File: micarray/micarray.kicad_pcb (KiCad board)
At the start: 4 copper layers, 75 x 75 mm, 36 parts, among them IC1 74LCX125MTCX, J1 Previous, J2 Next, J3 MCHStreamer J3

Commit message: mounting hole
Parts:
- added C11: 20p, Capacitor_SMD:C_0603_1608Metric_Pad1.08x0.95mm_HandSolder, F.Cu at (90.7, 61.6)
- J3: footprint Connector_PinHeader_2.54mm:PinHeader_2x06_P2.54mm_Horizontal -> Connector_PinHeader_2.54mm:PinHeader_2x06_P2.54mm_Vertical
- moved C6 11.0 mm to (120.9, 42.6), turned to -90 degrees
- moved C5 10.6 mm to (119.4, 42.6), turned to -90 degrees
- moved L3 10.5 mm to (117.9, 42.6), turned to 90 degrees
- moved R5 0.83 mm to (117.8, 46.2)
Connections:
- C1 pad 2: Net-(MK1-SELECT) -> Net-(MK1-VDD)
- C2 pad 2: Net-(MK1-SELECT) -> Net-(MK1-VDD)
- C3 pad 2: Net-(MK2-VDD) -> Net-(MK2-SELECT)
- C4 pad 2: Net-(MK2-VDD) -> Net-(MK2-SELECT)
- C5 pad 2: Net-(MK3-SELECT) -> Net-(MK3-VDD)
- C6 pad 2: Net-(MK3-SELECT) -> Net-(MK3-VDD)
- C7 pad 2: Net-(MK4-VDD) -> Net-(MK4-SELECT)
- C8 pad 2: Net-(MK4-VDD) -> Net-(MK4-SELECT)
- L1 pad 1: Net-(MK1-SELECT) -> Net-(MK1-VDD)
- L2 pad 1: Net-(MK2-VDD) -> Net-(MK2-SELECT)
- L3 pad 1: Net-(MK3-SELECT) -> Net-(MK3-VDD)
- L4 pad 1: Net-(MK4-VDD) -> Net-(MK4-SELECT)
- MK1 pad 2: Net-(MK1-SELECT) -> GND
- MK1 pad 5: Net-(MK1-SELECT) -> Net-(MK1-VDD)
- MK2 pad 2: GND -> Net-(MK2-SELECT)
- MK2 pad 5: Net-(MK2-VDD) -> Net-(MK2-SELECT)
- MK3 pad 2: Net-(MK3-SELECT) -> GND
- MK3 pad 5: Net-(MK3-SELECT) -> Net-(MK3-VDD)
- MK4 pad 2: GND -> Net-(MK4-SELECT)
- MK4 pad 5: Net-(MK4-VDD) -> Net-(MK4-SELECT)
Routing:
- net Net-(MK4-SELECT): track 0.00 -> 8.25 mm
- net Net-(MK3-SELECT): track 7.92 -> 0.00 mm
- net Net-(MK3-VDD): track 0.00 -> 7.69 mm
- net Net-(MK1-SELECT): track 7.61 -> 0.00 mm
- net Net-(MK2-SELECT): track 0.00 -> 7.19 mm
- net Net-(MK4-VDD): track 6.29 -> 0.00 mm
- net Net-(MK1-VDD): track 0.00 -> 5.62 mm
- net Net-(MK2-VDD): track 5.10 -> 0.00 mm
- net GND: track 39.7 -> 44.2 mm
- net PDM_DATA0: track 109.1 -> 112.0 mm
- net PDM_CLK2: track 13.1 -> 11.8 mm
- net +3V3: track 15.4 -> 14.5 mm, vias 19 -> 16
- added copper zone on In2.Cu, net +3V3
- removed copper zone on In2.Cu, net GND
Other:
- outline, holes or cut-outs redrawn
- board text added: "M3 MOUNT"

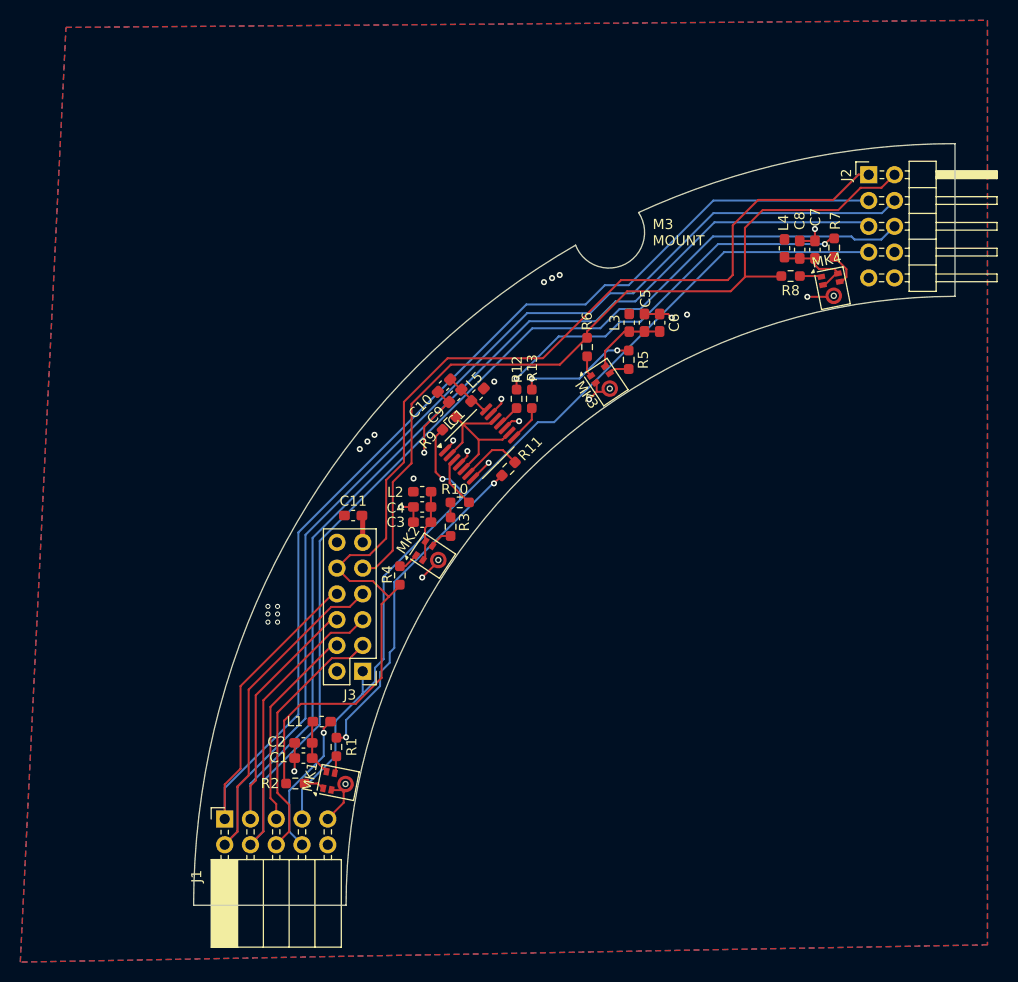
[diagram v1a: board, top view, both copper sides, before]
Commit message: 8ch progress, new mics for 16ch
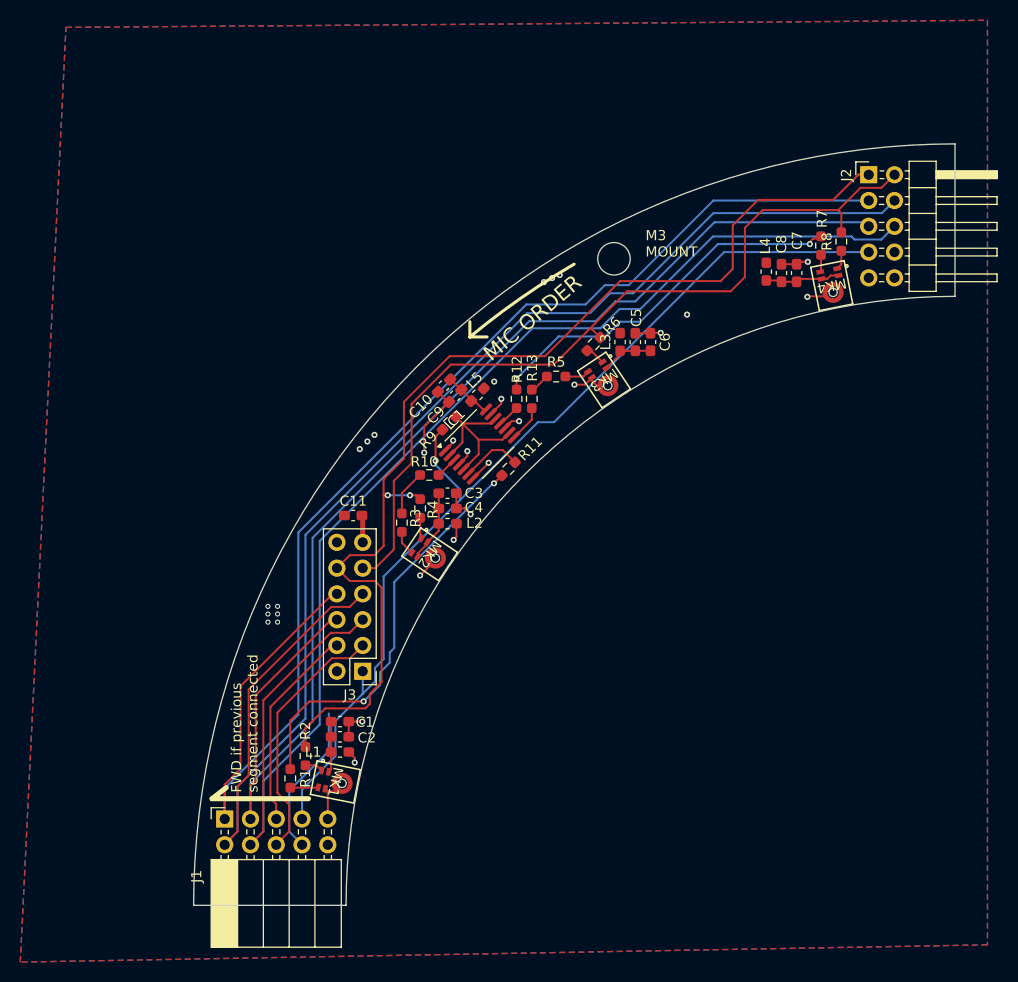
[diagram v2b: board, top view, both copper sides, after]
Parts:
- MK1, MK2, MK3, MK4: value SPH1668LM4H-1 -> IM73D122V01XTMA1; footprint Sensor_Audio:Knowles_LGA-5_3.5x2.65mm -> ul_IM73D122V01XTMA1:PG-LLGA-5-2_INF
- moved R5 7.34 mm to (110.7, 47.9), turned to 0 degrees
- moved R4 6.90 mm to (97.3, 60.9), turned to 90 degrees
- moved R8 6.05 mm to (138.8, 34.6), turned to 90 degrees
- moved R1 5.51 mm to (84.5, 87.5)
- moved C1 5.09 mm to (89.4, 81.9), turned to 180 degrees
- moved R3 4.82 mm to (95.5, 62.3)
- moved R10 4.04 mm to (98.2, 57.6)
- moved L2 4.02 mm to (100.0, 62.4), turned to 0 degrees
- moved C3 3.79 mm to (100.0, 59.4), turned to 180 degrees
- moved C2 3.65 mm to (89.4, 83.4), turned to 180 degrees
- moved L1 3.50 mm to (89.4, 84.9)
- moved C7 2.92 mm to (134.4, 37.7)
- moved C8 2.92 mm to (132.9, 37.7)
- moved L4 2.92 mm to (131.4, 37.6)
- moved R2 2.88 mm to (86.0, 85.3), turned to 90 degrees
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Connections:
- C3 pad 2: Net-(MK2-SELECT) -> Net-(MK2-LR)
- C4 pad 2: Net-(MK2-SELECT) -> Net-(MK2-LR)
- C7 pad 2: Net-(MK4-SELECT) -> Net-(MK4-LR)
- C8 pad 2: Net-(MK4-SELECT) -> Net-(MK4-LR)
- L2 pad 1: Net-(MK2-SELECT) -> Net-(MK2-LR)
- L4 pad 1: Net-(MK4-SELECT) -> Net-(MK4-LR)
- MK1 pad 2: GND -> Net-(MK1-VDD)
- MK1 pad 3: GND -> Net-(MK1-CLOCK)
- MK1 pad 4: Net-(MK1-CLOCK) -> GND
- MK1 pad 5: Net-(MK1-VDD) -> GND
- MK2 pad 2: Net-(MK2-SELECT) -> Net-(MK2-LR)
- MK2 pad 3: GND -> Net-(MK2-CLOCK)
- MK2 pad 4: Net-(MK2-CLOCK) -> Net-(MK2-LR)
- MK2 pad 5: Net-(MK2-SELECT) -> GND
- MK3 pad 2: GND -> Net-(MK3-VDD)
- MK3 pad 3: GND -> Net-(MK3-CLOCK)
- MK3 pad 4: Net-(MK3-CLOCK) -> GND
- MK3 pad 5: Net-(MK3-VDD) -> GND
- MK4 pad 2: Net-(MK4-SELECT) -> Net-(MK4-LR)
- MK4 pad 3: GND -> Net-(MK4-CLOCK)
- MK4 pad 4: Net-(MK4-CLOCK) -> Net-(MK4-LR)
- MK4 pad 5: Net-(MK4-SELECT) -> GND
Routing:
- net PDM_CLK2: track 11.8 -> 2.02 mm, vias 2 -> 0
- net Net-(MK4-SELECT): track 8.25 -> 0.00 mm
- net PDM_CLK0: track 33.2 -> 40.8 mm
- net Net-(MK4-LR): track 0.00 -> 7.43 mm
- net Net-(MK2-SELECT): track 7.19 -> 0.00 mm
- net Net-(MK2-LR): track 0.00 -> 7.11 mm
- net +3V3: track 14.5 -> 18.2 mm
- net PDM_DATA0: track 112.0 -> 108.3 mm, vias 0 -> 2
- net PDM_CLK1: track 1.49 -> 4.53 mm
- net Net-(IC1-O0): track 5.18 -> 2.17 mm
- net Net-(MK3-VDD): track 7.69 -> 5.25 mm
- net GND: track 44.2 -> 46.2 mm
- net Net-(MK4-CLOCK): track 3.33 -> 1.71 mm
- net Net-(MK1-CLOCK): track 1.64 -> 2.77 mm
- net PDM_CLK3: track 38.1 -> 37.0 mm
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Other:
- outline, holes or cut-outs redrawn
- board text added: "FWD if previous segment connected"
- board text added: "MIC ORDER"

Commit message: 16ch V2 ordered
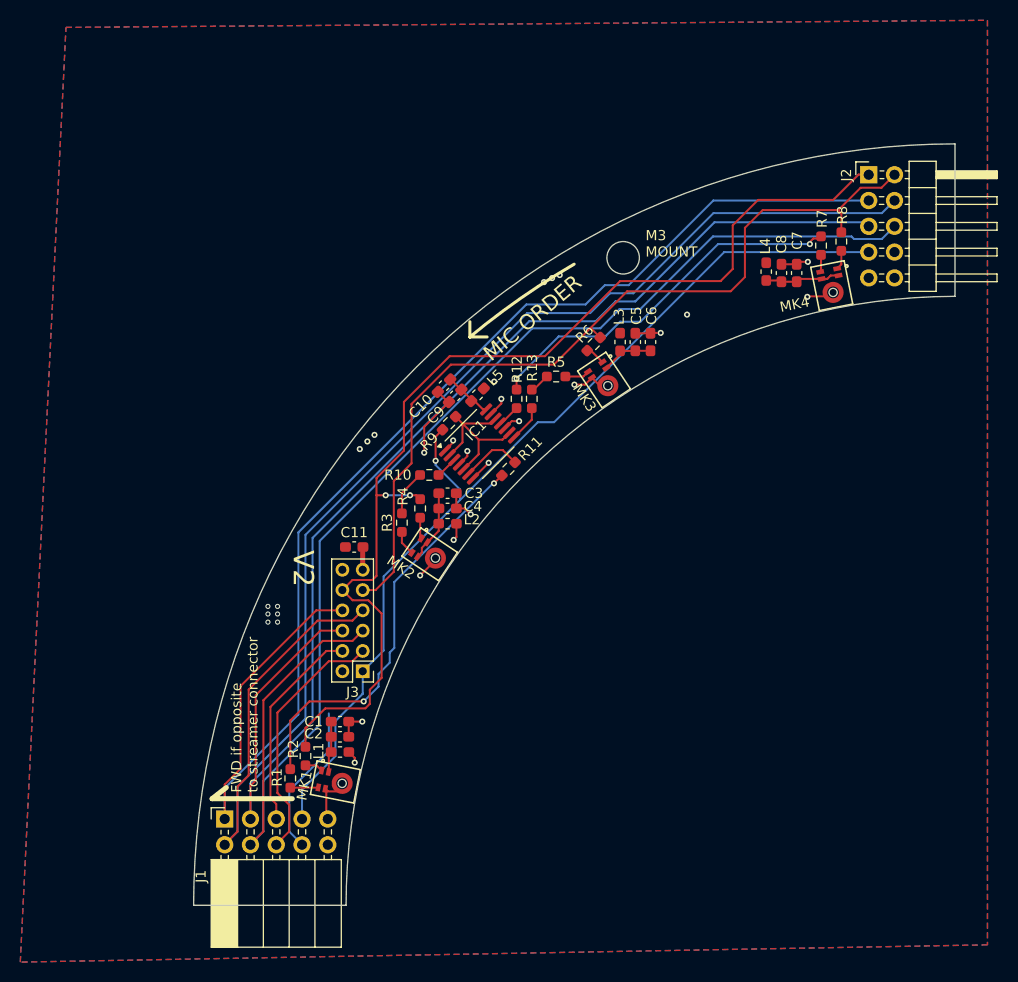
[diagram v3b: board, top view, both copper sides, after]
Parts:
- J3: footprint Connector_PinHeader_2.54mm:PinHeader_2x06_P2.54mm_Vertical -> Connector_PinHeader_2.00mm:PinHeader_2x06_P2.00mm_Vertical
- moved C11 3.10 mm to (90.8, 64.7)
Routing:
- net PDM_CLK-IN: track 98.4 -> 96.2 mm
- net PDM_DATA1: track 82.4 -> 84.5 mm
- net PDM_DATA3: track 136.9 -> 136.2 mm
- net PDM_DATA0: track 108.3 -> 107.7 mm
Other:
- outline, holes or cut-outs redrawn
- board text added: "FWD if opposite to streamer connector"
- board text added: "V2"
- board text removed: "FWD if previous segment connected"

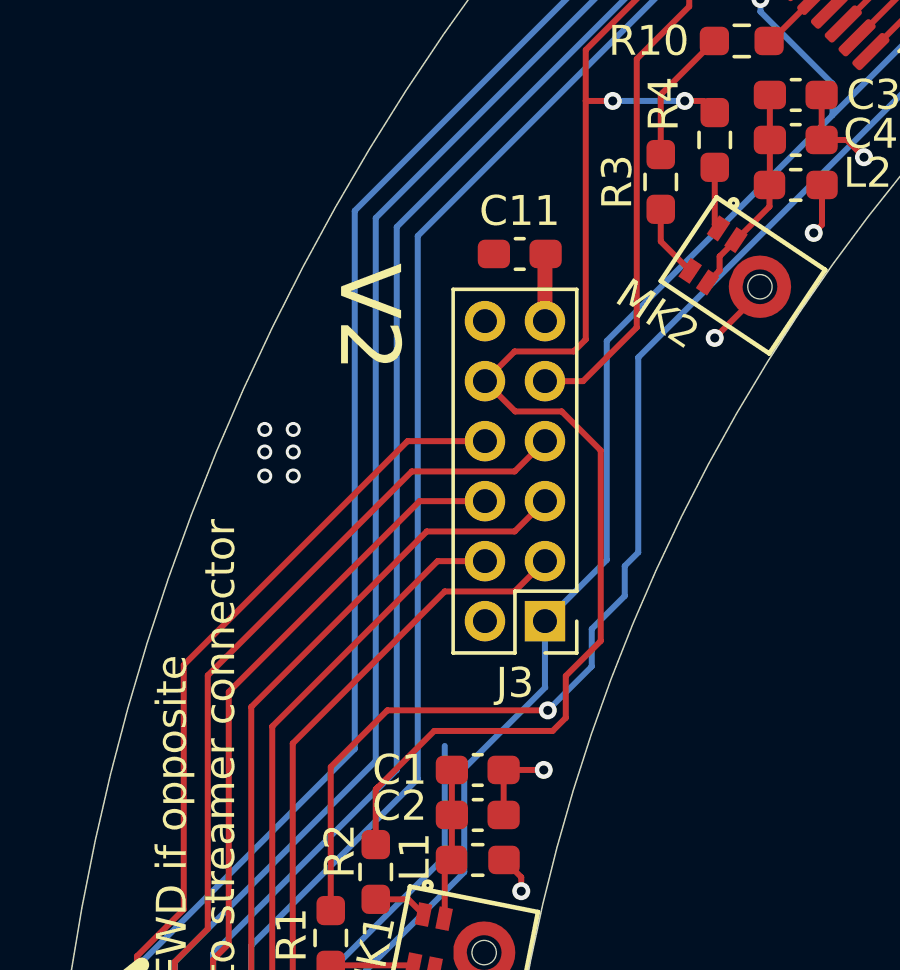
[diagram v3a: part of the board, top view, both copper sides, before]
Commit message: Clock line capacitor was in the wrong place
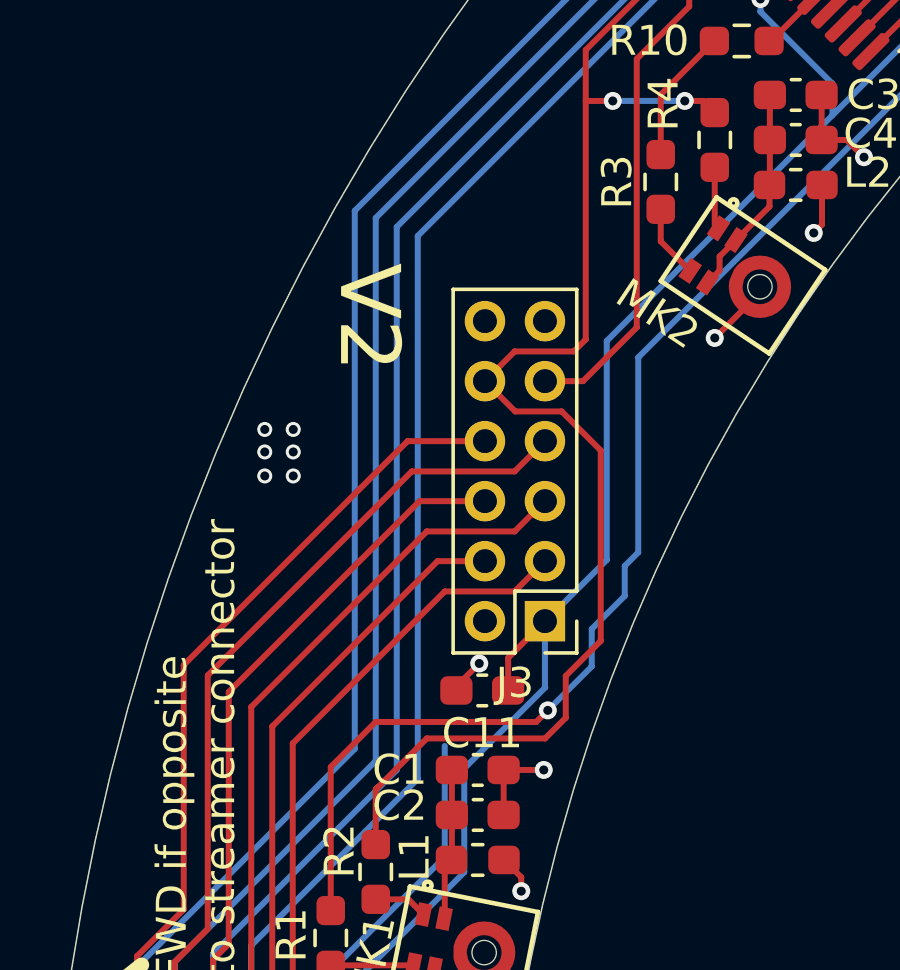
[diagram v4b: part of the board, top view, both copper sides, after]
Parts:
- moved C11 14.6 mm to (89.5, 79.2), turned to 180 degrees
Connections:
- C11 pad 1: +3V3 -> PDM_CLK-IN
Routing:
- net PDM_CLK-IN: track 96.2 -> 99.0 mm
- net GND: track 46.2 -> 45.1 mm, vias 13 -> 14

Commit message: Cleanup, library move
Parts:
- C11: value 20p -> 150p
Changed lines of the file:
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@@
 			)
 		)
-		(property "Value" "20p"
+		(property "Value" "150p"
 			(at 0 1.43 180)
 			(layer "F.Fab")
@@
 			)
 		)
-		(property "LCSC Part #" "C126554"
+		(property "LCSC Part #" "C37298"
 			(at 0 0 180)
 			(unlocked yes)
